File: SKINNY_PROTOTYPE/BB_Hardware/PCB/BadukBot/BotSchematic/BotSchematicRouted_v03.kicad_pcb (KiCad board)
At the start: 2 copper layers, 93.5 x 43.6 mm, 118 parts, among them J1 MOLEX781710002, J10 A316DA2SV71, J11 62401621722, J12 A316DA2SV71, J13 0877601616, J2 MOLEX781710003, M1 Pos1a, M2 Neg1a, M3 Pos2a, M4 Neg2a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

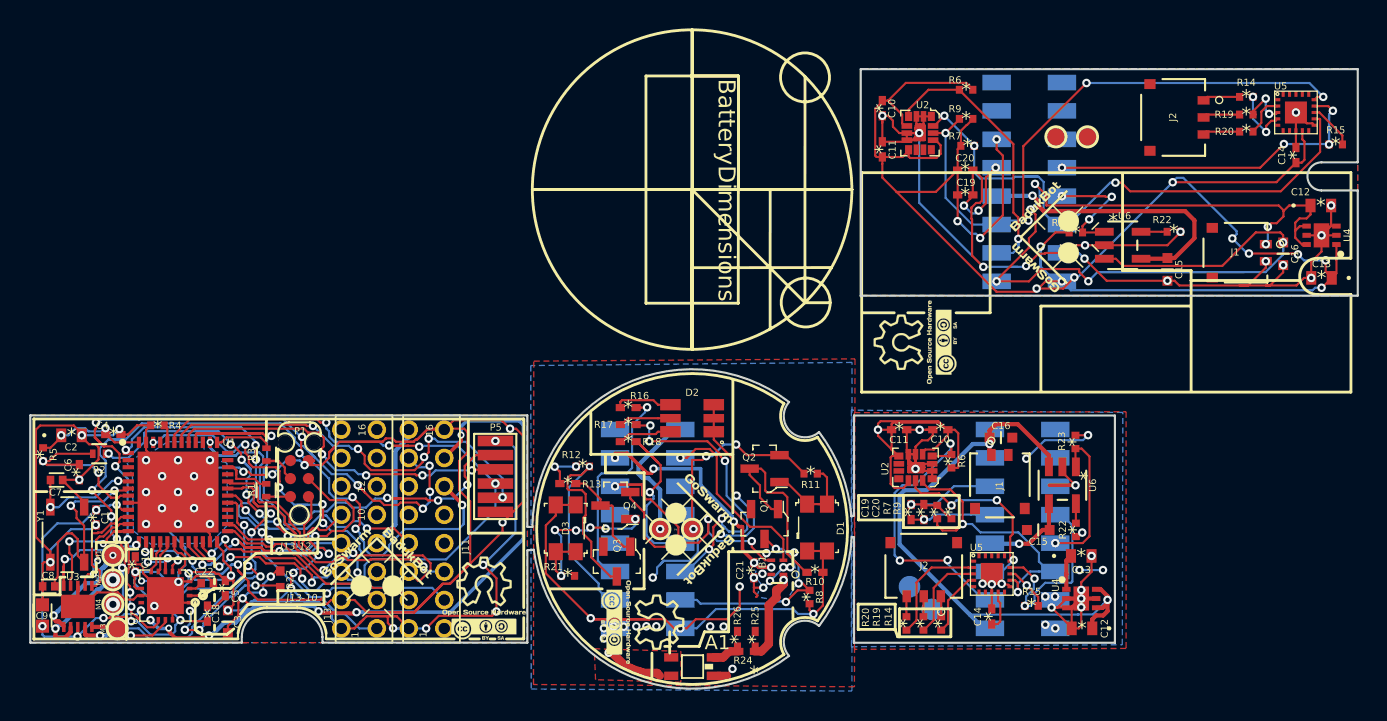
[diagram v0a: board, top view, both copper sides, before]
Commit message: Changed PCB for more compact component placement, shortened board 3, added images for the new layout
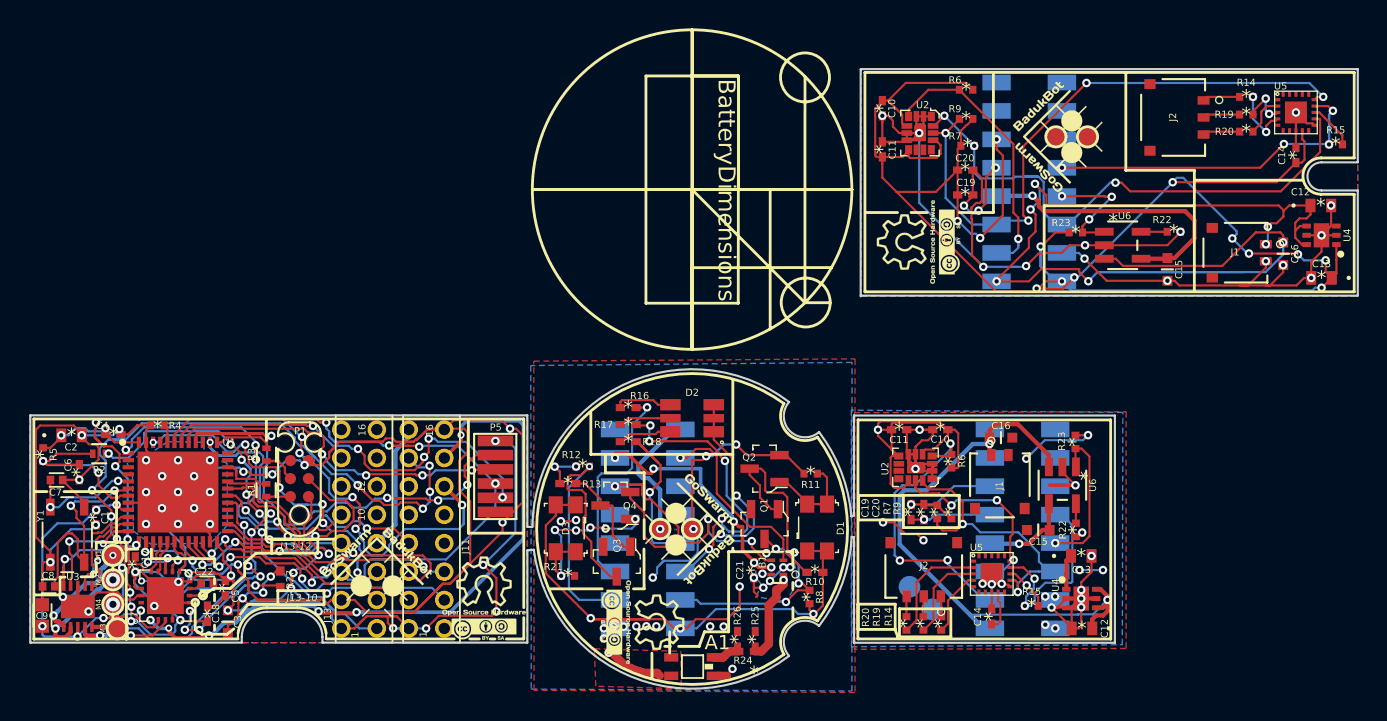
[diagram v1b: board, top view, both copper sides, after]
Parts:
- moved G2 7.06 mm to (132.2, 87.5)
- moved G1 7.06 mm to (142.1, 80.2)
- renumbered P4 to P10
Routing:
- net 23aGround: track 123.9 -> 127.2 mm, vias 29 -> 31
- net 4aPHOTODIODE2: track 22.8 -> 24.0 mm
- net 1a33v: track 62.0 -> 63.0 mm, vias 8 -> 10
- net 2bGND: vias 29 -> 31

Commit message: Reduced board sizes, results in $6 saved per 3 boards at OSHPark
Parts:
- removed the C10 at (129.7, 78.1)
- removed the C11 at (129.7, 81.0)
- removed the C12 at (160.5, 85.0)
- removed the C13 at (160.6, 90.1)
- removed the C14 at (158.8, 81.4)
- removed the C15 at (149.7, 89.5)
- removed the C16 at (157.9, 88.4)
- removed the C19 at (135.5, 84.2)
- removed the C20 at (135.5, 82.5)
- removed the G1 at (142.1, 80.2)
- removed the G2 at (132.2, 87.5)
- removed the J1 at (154.5, 88.3)
- removed the J12 at (140.6, 83.3)
- removed the J2 at (150.1, 78.8)
- removed the R14 at (155.3, 77.3)
- removed the R15 at (161.6, 80.7)
- removed the R19 at (155.3, 78.6)
- removed the R20 at (155.3, 79.8)
- removed the R22 at (150.2, 86.8)
- removed the R23 at (143.3, 86.9)
- removed the R6 at (135.6, 76.8)
- removed the R7 at (135.7, 80.8)
- removed the R9 at (135.6, 78.9)
- removed TESTPOINT-50MIL (x2): VAL**, gsg-modules:TESTPOINT-50MIL
- removed the U2 at (132.3, 79.9)
- removed the U4 at (160.6, 87.1)
- removed the U5 at (158.8, 78.4)
- removed the U6 at (146.6, 87.8)
- G1, G2: moved to B.Cu
- J13: value 0877601616 -> 62401621722
- moved G2 18.5 mm to (85.1, 104.4), turned to 90 degrees
- moved G1 17.3 mm to (77.9, 104.6), turned to 90 degrees
- moved P5 17.2 mm to (117.0, 113.1), turned to 180 degrees
- moved G5 3.97 mm to (83.7, 110.1)
- moved C1 3.38 mm to (77.7, 106.9)
- moved C4 3.38 mm to (78.9, 101.1)
- moved C5 3.38 mm to (86.8, 111.9)
- moved C7 3.38 mm to (74.9, 104.3)
- moved C8 3.38 mm to (74.4, 111.8)
- moved M3 3.38 mm to (79.2, 114.8)
- moved M4 3.38 mm to (78.9, 113.1)
- moved R1 3.38 mm to (89.7, 105.0)
- moved R2 3.38 mm to (77.9, 102.5)
- moved Y1 3.38 mm to (75.7, 108.2)
- moved C17 3.38 mm to (80.5, 110.2)
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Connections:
- J10 pad 16: Net-(J10-Pad16) -> 2aGND
- J11 pad 10: Net-(J11-Pad10) -> 8bIO1
- J11 pad 11: Net-(J11-Pad11) -> 9bIO2
- J11 pad 8: Net-(J11-Pad8) -> 11bSCL
- J11 pad 9: Net-(J11-Pad9) -> 10bSDA
- P5 pad 1: 1b33v -> 1a33v
- P5 pad 2: 8bIO1 -> Net-(J10-Pad10)
- P5 pad 3: 9bIO2 -> Net-(J10-Pad11)
- P5 pad 4: 10bSDA -> Net-(J10-Pad9)
- P5 pad 5: 11bSCL -> Net-(J10-Pad8)
- P5 pad 6: 2bGND -> 2aGND
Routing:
- net 21a33v: track 158.4 -> 47.8 mm, vias 20 -> 9
- net 22aVBAT: track 129.7 -> 43.7 mm, vias 9 -> 2
- net 23aGround: track 127.2 -> 53.8 mm, vias 31 -> 16
- net 26aSCL: track 57.1 -> 14.0 mm, vias 7 -> 3
- net 25aSDA: track 63.3 -> 21.2 mm, vias 5 -> 2
- net 23a_Ground: track 31.3 -> 3.87 mm
- net ~29aTOUCHCHG~: track 40.2 -> 14.1 mm, vias 6 -> 2
- net 28aP41: track 27.8 -> 6.50 mm, vias 2 -> 1
- net 1b33v: track 123.3 -> 103.4 mm, vias 22 -> 19
- net 24aIMUINT: track 40.0 -> 20.4 mm, vias 4 -> 3
- net 2bGND: track 173.1 -> 153.6 mm, vias 31 -> 29
- net 1a33v: track 63.0 -> 46.2 mm, vias 10 -> 9
- net Net-(J10-Pad11): track 0.00 -> 16.2 mm, vias 0 -> 3
- net 21a_3.3v: track 16.5 -> 2.78 mm
- net Net-(J10-Pad10): track 0.00 -> 12.8 mm, vias 0 -> 1
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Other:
- board size 93.5 x 43.6 mm -> 73 x 22.5 mm
- board text added: "3.3v"
- board text added: "GND"
- board text added: "IO1"
- board text added: "IO2"
- board text added: "SCL"
- board text added: "SDA"
